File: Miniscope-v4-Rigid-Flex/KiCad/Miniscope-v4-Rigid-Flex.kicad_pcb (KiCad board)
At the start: 6 copper layers, 30 x 57.3 mm, 111 parts, among them J1 DNL, J11 DNL, J12 DNL, J17 U.FL-R-SMT-1(10), J2 DNL, J3 DNL, J4 DNL, J5 DNL, J6 DNL, J9 DNL, Q1 MMBT3904LP-7B, U1 ATmega328-MU, U10 NCP163AMX330TBG, U11 PCA9509AGM, U12 BNO055, U2 LTC3218, U3 TPL0102-100RUCR, U4 MAX14574EWL+, U5 LMV321IDCKR, U6 NOIP1SP0480A, U7 SG-210STF 66.6667ML3, U8 TLV7103318DSER, U9 DS90UB913ATRTVTQ1

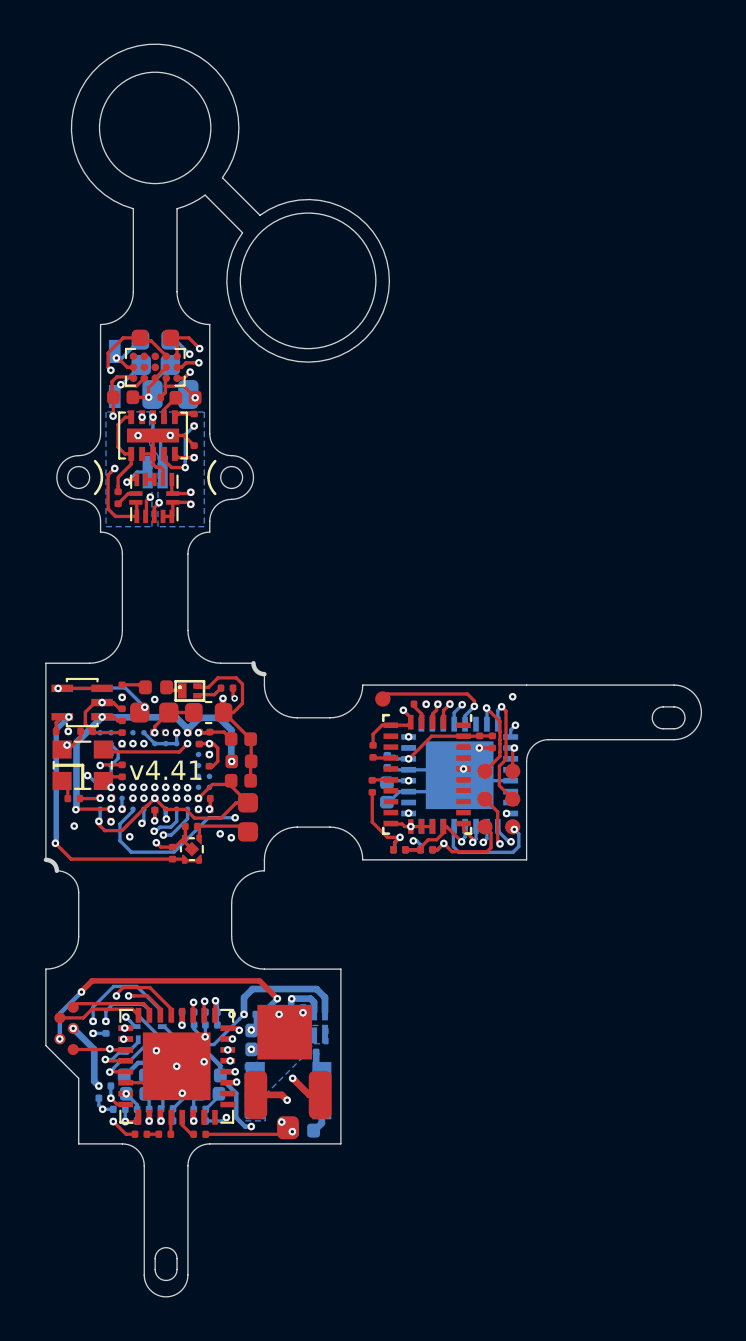
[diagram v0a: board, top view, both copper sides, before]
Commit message: Updated PCB project for modern KiCAD compatibility
- Removed the dependency on the deprecated Aharoni Lab KiCAD library
- Now all symbols load correctly, and are stored in a project based folder
- Created a library for footprints
- Fixed the path for all 3D models by creating a folder within the repository (3D Models) and linked all the 3D models using relative paths (${KIPRJMOD}/3D Models)
- Verified that everything is in place. Tested using KiCAD version 9.0.2
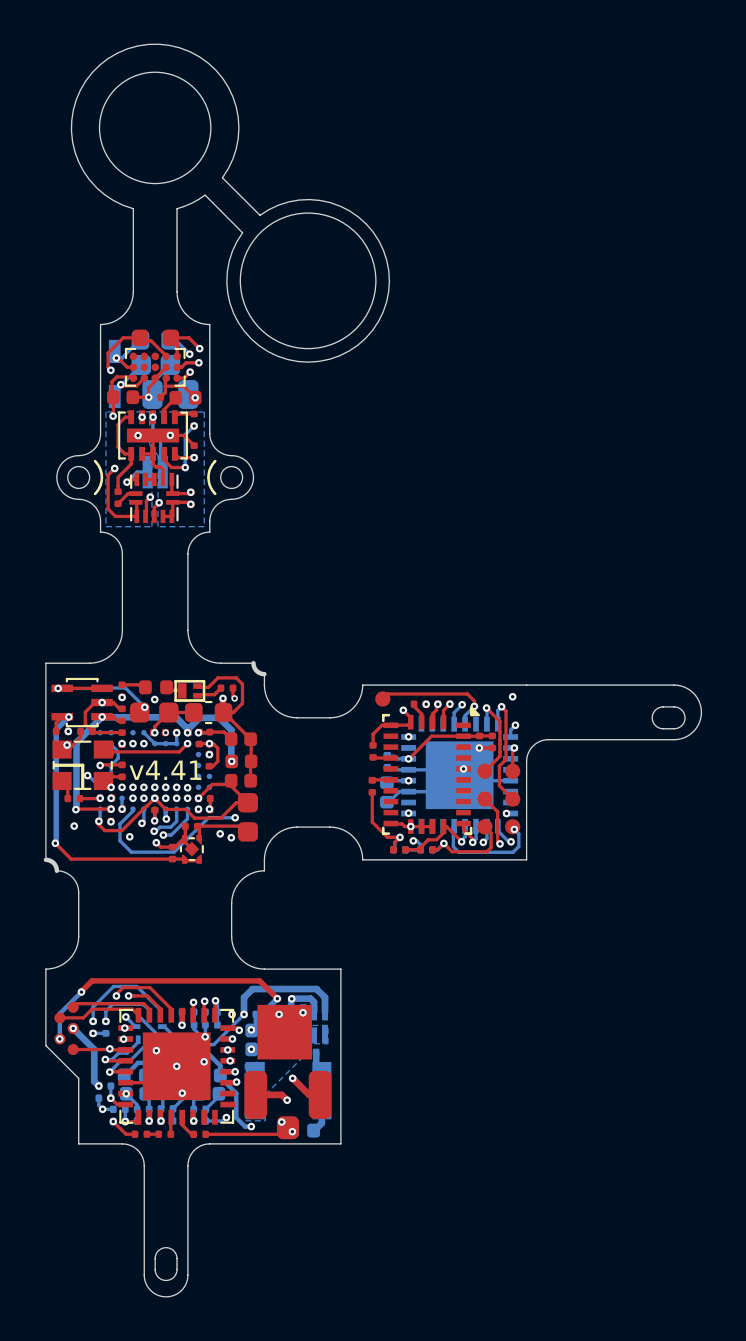
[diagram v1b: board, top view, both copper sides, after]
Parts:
- C1, C10, C11, C12, C13, C14, C16, C17, C18, C20, C21, C22, C24, C25, C26, C28, C3, C31, C32, C33, C34, C35, C37, C38, C4, C40, C41, C42, C44, C45, C46, C47, C48, C49, C51, C52, C53, C54, C55, C56, C57, C58, C6, C8: footprint .Capacitor:C_0201_0603Metric_L -> Miniscope_V4_library:C_0201_0603Metric_L
- C15, C19, C2, C23, C29, C30, C36, C39, C43, C5, C7: footprint .Capacitor:C_0402_1005Metric_L -> Miniscope_V4_library:C_0402_1005Metric_L
- C27, C9: footprint .Capacitor:C_0603_1608Metric_L -> Miniscope_V4_library:C_0603_1608Metric_L
- C50: footprint .Capacitor:C_0805_2012Metric_L -> Miniscope_V4_library:C_0805_2012Metric_L
- D1: footprint .LED:LED_LXZ1_PB01_L -> Miniscope_V4_library:LED_LXZ1_PB01_L
- D2: footprint .Diode:SOD_323_250X125X110L30X32L -> Miniscope_V4_library:SOD_323_250X125X110L30X32L
- D3: footprint LED_SMD:LED_0402_1005Metric -> Miniscope_V4_library:LED_0402_1005Metric
- HOLE (x2): footprint .Connector:Conn_1x1_100x100_Pad -> Miniscope_V4_library:Conn_1x1_100x100_Pad
- J17: footprint .Connector:U-FL-R-SMT -> Miniscope_V4_library:U-FL-R-SMT
- L1, L2, L3: footprint .Inductor:L_0603_1608Metric_L -> Miniscope_V4_library:L_0603_1608Metric_L
- L5: footprint .Inductor:L_1210_3225Metric_L -> Miniscope_V4_library:L_1210_3225Metric_L
- Q1: footprint .Transistor:TRXDFN3_101X61X53L25X15N -> Miniscope_V4_library:TRXDFN3_101X61X53L25X15N
- R1, R10, R11, R12, R13, R14, R15, R16, R2, R3, R4, R5, R6, R7, R8, R9: footprint .Resistor:R_0201_0603Metric_ERJ_L -> Miniscope_V4_library:R_0201_0603Metric_ERJ_L
- U1, U9: footprint .Package_QFN:QFN_33_P50_500X500X80L40X24T310L -> Miniscope_V4_library:QFN_33_P50_500X500X80L40X24T310L
- U10: footprint .Package_QFN:UQFN_MCP1711 -> Miniscope_V4_library:XDFN-ncp163
- U11: footprint .Package_QFN:XQFN8 -> Miniscope_V4_library:XQFN8
- U2: footprint .Package_SON:SON_11_P50_300X200X80L40X25T239X64L -> Miniscope_V4_library:SON_11_P50_300X200X80L40X25T239X64L
- U3: footprint .Package_QFN:QFN_14_P40_200X200X40L40X20L -> Miniscope_V4_library:QFN_14_P40_200X200X40L40X20L
- U4: footprint .Package_BGA:BGA_15_NP50_3X5_155X255X69B31N -> Miniscope_V4_library:BGA_15_NP50_3X5_155X255X69B31N
- U5: footprint .Package_SOT:SOT_23-5P65_210X110L36X22L -> Miniscope_V4_library:SOT_23-5P65_210X110L36X22L
- U6: footprint .Package_BGA:BGA88CP50_8X11_493X613X75B25 -> Miniscope_V4_library:BGA88CP50_8X11_493X613X75B25
- U7: footprint .Oscillator:OSC_CC250X200X80L70X75L -> Miniscope_V4_library:OSC_CC250X200X80L70X75L
- U8: footprint .Package_SON:SON_6_P50_150X150X80L50X25L -> Miniscope_V4_library:SON_6_P50_150X150X80L50X25L
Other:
- net class Default removed
